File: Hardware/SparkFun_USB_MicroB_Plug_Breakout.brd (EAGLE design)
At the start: 22.9 x 14 mm, 3 parts

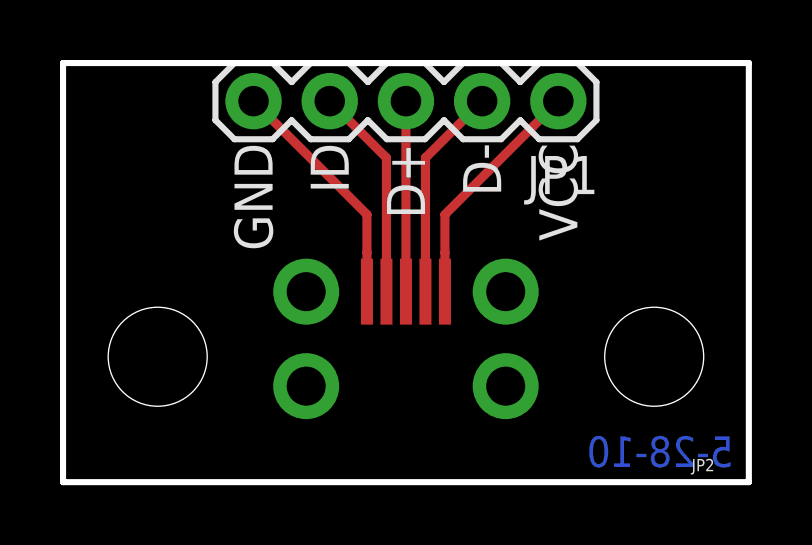
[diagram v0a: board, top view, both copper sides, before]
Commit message: Fixed USB Micro footprint.  Added OSHW SPK logo
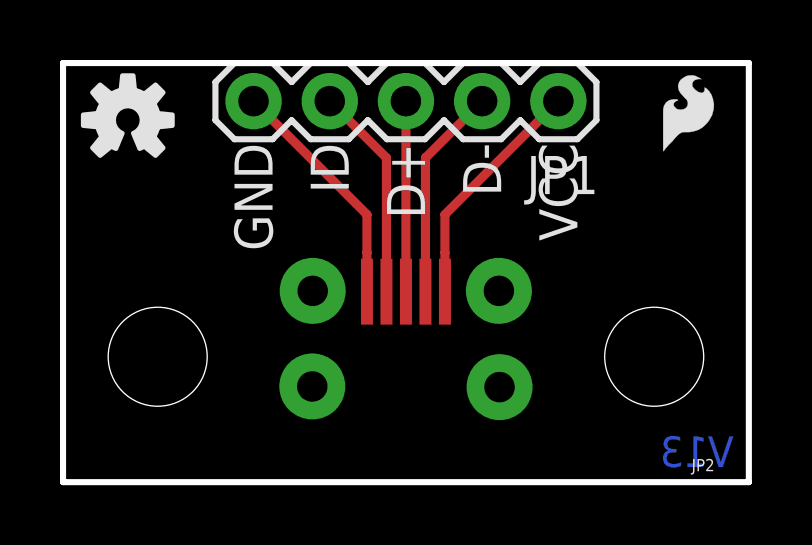
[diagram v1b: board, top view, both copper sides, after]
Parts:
- removed JP3: LOGO-SFESK, SparkFun:SFE-LOGO-FLAME
- added FRAME1: FRAME-LETTER, SparkFun-Aesthetics:CREATIVE_COMMONS
- added LOGO1: OSHW-LOGOS, SparkFun-Aesthetics:OSHW-LOGO-S
- added LOGO2: SFE_LOGO_FLAME.1_INCH, SparkFun-Aesthetics:SFE_LOGO_FLAME_.1
- JP2: value USB_MICROB_PLUG-SMT -> (none); device SparkFun:MICRO-B-SMT -> SparkFun-Connectors:MICRO-B-SMT
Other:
- board text added: "Breakout"
- board text added: "USB MicroB Plug"
- board text added: "V13"
- board text removed: "5-28-10"
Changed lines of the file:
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@@
 <?xml version="1.0" encoding="utf-8"?>
 <!DOCTYPE eagle SYSTEM "eagle.dtd">
-<eagle version="7.2.0">
+<eagle version="7.1.0">
 <drawing>
 <settings>
@@
 <layer number="54" name="bGND_GNDA" color="1" fill="9" visible="no" active="no"/>
 <layer number="56" name="wert" color="7" fill="1" visible="no" active="yes"/>
+<layer number="57" name="tCAD" color="7" fill="1" visible="no" active="no"/>
+<layer number="59" name="tCarbon" color="7" fill="1" visible="no" active="no"/>
+<layer number="60" name="bCarbon" color="7" fill="1" visible="no" active="no"/>
+<layer number="90" name="Modules" color="5" fill="1" visible="no" active="no"/>
 <layer number="91" name="Nets" color="2" fill="1" visible="no" active="no"/>
 <layer number="92" name="Busses" color="1" fill="1" visible="no" active="no"/>
@@
 <layer number="97" name="Info" color="7" fill="1" visible="no" active="no"/>
 <layer number="98" name="Guide" color="6" fill="1" visible="no" active="no"/>
+<layer number="99" name="SpiceOrder" color="7" fill="1" visible="no" active="no"/>
 <layer number="100" name="Muster" color="7" fill="1" visible="no" active="no"/>
 <layer number="101" name="Patch_Top" color="12" fill="4" visible="no" active="yes"/>
@@
 <layer number="106" name="bPlate" color="7" fill="1" visible="no" active="yes"/>
 <layer number="107" name="Crop" color="7" fill="1" visible="no" active="yes"/>
+<layer number="108" name="tplace-old" color="10" fill="1" visible="no" active="yes"/>
+<layer number="109" name="ref-old" color="11" fill="1" visible="no" active="yes"/>
+<layer number="110" name="fp0" color="7" fill="1" visible="no" active="yes"/>
+<layer number="111" name="LPC17xx" color="7" fill="1" visible="no" active="yes"/>
+<layer number="112" name="tSilk" color="7" fill="1" visible="no" active="yes"/>
+<layer number="113" name="IDFDebug" color="4" fill="1" visible="no" active="yes"/>
 <layer number="116" name="Patch_BOT" color="9" fill="4" visible="no" active="yes"/>
 <layer number="121" name="_tsilk" color="7" fill="1" visible="no" active="yes"/>
 <layer number="122" name="_bsilk" color="7" fill="1" visible="no" active="yes"/>
+<layer number="123" name="tTestmark" color="7" fill="1" visible="no" active="yes"/>
+<layer number="124" name="bTestmark" color="7" fill="1" visible="no" active="yes"/>
+<layer number="125" name="_tNames" color="7" fill="1" visible="no" active="yes"/>
+<layer number="126" name="_bNames" color="7" fill="1" visible="no" active="yes"/>
+<layer number="127" name="_tValues" color="7" fill="1" visible="no" active="yes"/>
+<layer number="128" name="_bValues" color="7" fill="1" visible="no" active="yes"/>
+<layer number="129" name="Mask" color="7" fill="1" visible="no" active="yes"/>
+<layer number="131" name="tAdjust" color="7" fill="1" visible="no" active="yes"/>
+<layer number="132" name="bAdjust" color="7" fill="1" visible="no" active="yes"/>
+<layer number="144" name="Drill_legend" color="7" fill="1" visible="no" active="yes"/>
+<layer number="150" name="Notes" color="7" fill="1" visible="no" active="yes"/>
 <layer number="151" name="HeatSink" color="7" fill="1" visible="no" active="yes"/>
+<layer number="152" name="_bDocu" color="7" fill="1" visible="no" active="yes"/>
+<layer number="153" name="FabDoc1" color="7" fill="1" visible="no" active="yes"/>
+<layer number="154" name="FabDoc2" color="7" fill="1" visible="no" active="yes"/>
+<layer number="155" name="FabDoc3" color="7" fill="1" visible="no" active="yes"/>
+<layer number="199" name="Contour" color="7" fill="1" visible="no" active="yes"/>
 <layer number="200" name="200bmp" color="1" fill="10" visible="no" active="yes"/>
 <layer number="201" name="201bmp" color="2" fill="10" visible="no" active="yes"/>
@@
 <layer number="207" name="207bmp" color="8" fill="10" visible="no" active="yes"/>
 <layer number="208" name="208bmp" color="9" fill="10" visible="no" active="yes"/>
+<layer number="209" name="209bmp" color="7" fill="1" visible="no" active="yes"/>
+<layer number="210" name="210bmp" color="7" fill="1" visible="no" active="yes"/>
+<layer number="211" name="211bmp" color="7" fill="1" visible="no" active="yes"/>
+<layer number="212" name="212bmp" color="7" fill="1" visible="no" active="yes"/>
+<layer number="213" name="213bmp" color="7" fill="1" visible="no" active="yes"/>
+<layer number="214" name="214bmp" color="7" fill="1" visible="no" active="yes"/>
+<layer number="215" name="215bmp" color="7" fill="1" visible="no" active="yes"/>
+<layer number="216" name="216bmp" color="7" fill="1" visible="no" active="yes"/>
+<layer number="217" name="217bmp" color="18" fill="1" visible="no" active="no"/>
+<layer number="218" name="218bmp" color="19" fill="1" visible="no" active="no"/>
+<layer number="219" name="219bmp" color="20" fill="1" visible="no" active="no"/>
+<layer number="220" name="220bmp" color="21" fill="1" visible="no" active="no"/>
+<layer number="221" name="221bmp" color="22" fill="1" visible="no" active="no"/>
+<layer number="222" name="222bmp" color="23" fill="1" visible="no" active="no"/>
+<layer number="223" name="223bmp" color="24" fill="1" visible="no" active="no"/>
+<layer number="224" name="224bmp" color="25" fill="1" visible="no" active="no"/>
+<layer number="225" name="225bmp" color="7" fill="1" visible="no" active="yes"/>
+<layer number="226" name="226bmp" color="7" fill="1" visible="no" active="yes"/>
+<layer number="227" name="227bmp" color="7" fill="1" visible="no" active="yes"/>
+<layer number="228" name="228bmp" color="7" fill="1" visible="no" active="yes"/>
+<layer number="229" name="229bmp" color="7" fill="1" visible="no" active="yes"/>
+<layer number="230" name="230bmp" color="7" fill="1" visible="no" active="yes"/>
+<layer number="231" name="231bmp" color="7" fill="1" visible="no" active="yes"/>
+<layer number="248" name="Housing" color="7" fill="1" visible="no" active="yes"/>
+<layer number="249" name="Edge" color="7" fill="1" visible="no" active="yes"/>
 <layer number="250" name="Descript" color="3" fill="1" visible="no" active="no"/>
 <layer number="251" name="SMDround" color="12" fill="11" visible="no" active="no"/>
 <layer number="254" name="cooling" color="7" fill="1" visible="no" active="yes"/>
+<layer number="255" name="routoute" color="7" fill="1" visible="no" active="yes"/>
 </layers>
 <board>
@@
 <text x="13.335" y="11.303" size="1.27" layer="21" font="vector" ratio="15" rot="R270">D-</text>
 <text x="15.875" y="11.303" size="1.27" layer="21" font="vector" ratio="15" rot="R270">VCC</text>
-<text x="22.352" y="0.508" size="1.016" layer="16" font="vector" ratio="15" rot="MR0">5-28-10</text>
+<text x="22.352" y="0.508" size="1.016" layer="16" font="vector" ratio="15" rot="MR0">V13</text>
 <text x="6.985" y="11.303" size="1.27" layer="22" font="vector" ratio="15" rot="MR270">GND</text>
 <text x="9.525" y="11.303" size="1.27" layer="22" font="vector" ratio="15" rot="MR270">ID</text>
@@
 <text x="14.605" y="11.303" size="1.27" layer="22" font="vector" ratio="15" rot="MR270">D-</text>
 <text x="17.145" y="11.303" size="1.27" layer="22" font="vector" ratio="15" rot="MR270">VCC</text>
+<text x="17.78" y="8.89" size="1.016" layer="22" font="vector" ratio="15" rot="MR0">USB MicroB Plug</text>
+<text x="14.732" y="7.747" size="1.016" layer="22" font="vector" ratio="15" rot="MR0">Breakout</text>
 </plain>
 <attributes>
@@
 <elements>
 <element name="JP1" library="SparkFun" package="1X05" value="" x="16.51" y="12.7" rot="R180"/>
-<element name="JP3" library="SparkFun" package="SFE-LOGO-FLAME" value="LOGO-SFESK" x="12.319" y="5.334" rot="MR0"/>
-<element name="JP2" library="SparkFun" package="MICRO-B-SMT" value="USB_MICROB_PLUG-SMT" x="11.43" y="6.35" rot="R180"/>
+<element name="JP2" library="SparkFun-Connectors" package="MICRO-B-SMT" value="" x="11.43" y="6.35" rot="R180"/>
+<element name="FRAME1" library="SparkFun-Aesthetics" package="CREATIVE_COMMONS" value="FRAME-LETTER" x="-15.36405625" y="-12.192"/>
+<element name="LOGO1" library="SparkFun-Aesthetics" package="OSHW-LOGO-S" value="OSHW-LOGOS" x="2.159" y="12.065"/>
+<element name="LOGO2" library="SparkFun-Aesthetics" package="SFE_LOGO_FLAME_.1" value="SFE_LOGO_FLAME.1_INCH" x="19.685" y="10.668"/>
 </elements>
 <signals>

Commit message: Added silk and prod attributes.
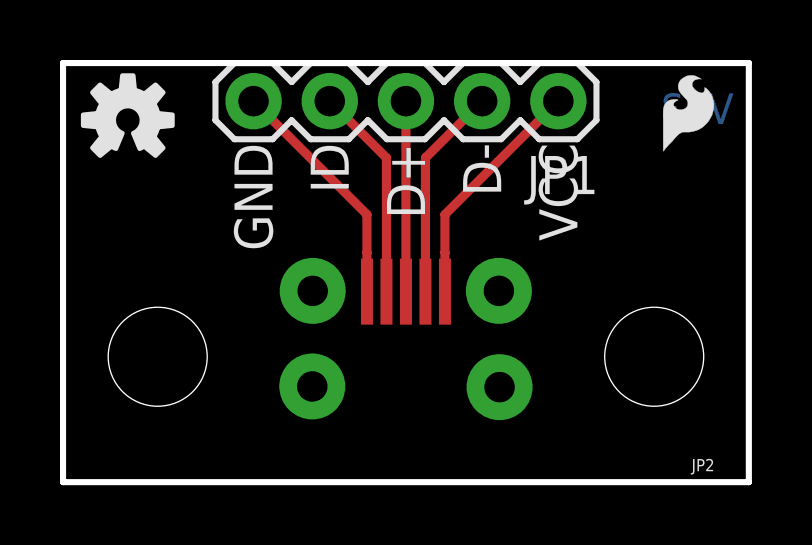
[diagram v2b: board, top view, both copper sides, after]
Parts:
- JP2: value (none) -> Micro B Plug
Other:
- board text added: "Jim Lindblom"
- board text added: "Revised by: Patrick Alberts"
- board text added: "USB MicroB Plug Breakout"
- board text removed: "Breakout"
- board text removed: "USB MicroB Plug"
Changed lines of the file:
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@@
 <layer number="23" name="tOrigins" color="15" fill="1" visible="yes" active="yes"/>
 <layer number="24" name="bOrigins" color="15" fill="1" visible="yes" active="yes"/>
-<layer number="25" name="tNames" color="7" fill="1" visible="no" active="yes"/>
+<layer number="25" name="tNames" color="7" fill="1" visible="yes" active="yes"/>
 <layer number="26" name="bNames" color="7" fill="1" visible="no" active="yes"/>
-<layer number="27" name="tValues" color="7" fill="1" visible="no" active="yes"/>
-<layer number="28" name="bValues" color="7" fill="1" visible="no" active="yes"/>
+<layer number="27" name="tValues" color="7" fill="1" visible="yes" active="yes"/>
+<layer number="28" name="bValues" color="7" fill="1" visible="yes" active="yes"/>
 <layer number="29" name="tStop" color="7" fill="3" visible="no" active="yes"/>
 <layer number="30" name="bStop" color="7" fill="6" visible="no" active="yes"/>
@@
 <text x="13.335" y="11.303" size="1.27" layer="21" font="vector" ratio="15" rot="R270">D-</text>
 <text x="15.875" y="11.303" size="1.27" layer="21" font="vector" ratio="15" rot="R270">VCC</text>
-<text x="22.352" y="0.508" size="1.016" layer="16" font="vector" ratio="15" rot="MR0">V13</text>
+<text x="22.352" y="11.938" size="1.016" layer="16" font="vector" ratio="15" rot="MR0">V13</text>
 <text x="6.985" y="11.303" size="1.27" layer="22" font="vector" ratio="15" rot="MR270">GND</text>
 <text x="9.525" y="11.303" size="1.27" layer="22" font="vector" ratio="15" rot="MR270">ID</text>
@@
 <text x="14.605" y="11.303" size="1.27" layer="22" font="vector" ratio="15" rot="MR270">D-</text>
 <text x="17.145" y="11.303" size="1.27" layer="22" font="vector" ratio="15" rot="MR270">VCC</text>
-<text x="17.78" y="8.89" size="1.016" layer="22" font="vector" ratio="15" rot="MR0">USB MicroB Plug</text>
-<text x="14.732" y="7.747" size="1.016" layer="22" font="vector" ratio="15" rot="MR0">Breakout</text>
+<text x="21.844" y="0.508" size="1.016" layer="22" font="vector" ratio="15" rot="MR0">USB MicroB Plug Breakout</text>
+<text x="-3.81" y="-15.24" size="1.778" layer="51" font="vector" ratio="10">Revised by: Patrick Alberts</text>
+<text x="14.732" y="-12.319" size="1.778" layer="51" font="vector" ratio="12">Jim Lindblom</text>
 </plain>
 <attributes>
@@
 <elements>
 <element name="JP1" library="SparkFun" package="1X05" value="" x="16.51" y="12.7" rot="R180"/>
-<element name="JP2" library="SparkFun-Connectors" package="MICRO-B-SMT" value="" x="11.43" y="6.35" rot="R180"/>
+<element name="JP2" library="SparkFun-Connectors" package="MICRO-B-SMT" value="Micro B Plug" x="11.43" y="6.35" rot="R180">
+<attribute name="PROD_ID" value="CONN-09900" x="11.43" y="6.35" size="1.778" layer="27" rot="R180" display="off"/>
+</element>
 <element name="FRAME1" library="SparkFun-Aesthetics" package="CREATIVE_COMMONS" value="FRAME-LETTER" x="-15.36405625" y="-12.192"/>
 <element name="LOGO1" library="SparkFun-Aesthetics" package="OSHW-LOGO-S" value="OSHW-LOGOS" x="2.159" y="12.065"/>

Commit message: Added Measures.
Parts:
- JP2: value Micro B Plug -> USB Micro B Plug
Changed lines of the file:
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@@
 <?xml version="1.0" encoding="utf-8"?>
 <!DOCTYPE eagle SYSTEM "eagle.dtd">
-<eagle version="7.1.0">
+<eagle version="6.4">
 <drawing>
 <settings>
@@
 <layer number="23" name="tOrigins" color="15" fill="1" visible="yes" active="yes"/>
 <layer number="24" name="bOrigins" color="15" fill="1" visible="yes" active="yes"/>
-<layer number="25" name="tNames" color="7" fill="1" visible="yes" active="yes"/>
+<layer number="25" name="tNames" color="7" fill="1" visible="no" active="yes"/>
 <layer number="26" name="bNames" color="7" fill="1" visible="no" active="yes"/>
-<layer number="27" name="tValues" color="7" fill="1" visible="yes" active="yes"/>
-<layer number="28" name="bValues" color="7" fill="1" visible="yes" active="yes"/>
+<layer number="27" name="tValues" color="7" fill="1" visible="no" active="yes"/>
+<layer number="28" name="bValues" color="7" fill="1" visible="no" active="yes"/>
 <layer number="29" name="tStop" color="7" fill="3" visible="no" active="yes"/>
 <layer number="30" name="bStop" color="7" fill="6" visible="no" active="yes"/>
@@
 <layer number="45" name="Holes" color="7" fill="1" visible="yes" active="yes"/>
 <layer number="46" name="Milling" color="3" fill="1" visible="no" active="yes"/>
-<layer number="47" name="Measures" color="7" fill="1" visible="no" active="yes"/>
+<layer number="47" name="Measures" color="7" fill="1" visible="yes" active="yes"/>
 <layer number="48" name="Document" color="7" fill="1" visible="no" active="yes"/>
 <layer number="49" name="Reference" color="7" fill="1" visible="no" active="yes"/>
@@
 <text x="-3.81" y="-15.24" size="1.778" layer="51" font="vector" ratio="10">Revised by: Patrick Alberts</text>
 <text x="14.732" y="-12.319" size="1.778" layer="51" font="vector" ratio="12">Jim Lindblom</text>
+<dimension x1="-3.81" y1="0" x2="-3.81" y2="13.97" x3="-5.08" y3="6.985" textsize="1.778" textratio="15" layer="47" unit="inch" visible="yes"/>
+<dimension x1="0" y1="17.78" x2="22.86" y2="17.78" x3="11.43" y3="16.51" textsize="1.778" textratio="15" layer="47" unit="inch" visible="yes"/>
 </plain>
 <attributes>
@@
 <pass name="Default">
 <param name="RoutingGrid" value="50mil"/>
-<param name="AutoGrid" value="1"/>
-<param name="Efforts" value="0"/>
-<param name="TopRouterVariant" value="1"/>
 <param name="tpViaShape" value="round"/>
 <param name="PrefDir.1" value="|"/>
@@
 <elements>
 <element name="JP1" library="SparkFun" package="1X05" value="" x="16.51" y="12.7" rot="R180"/>
-<element name="JP2" library="SparkFun-Connectors" package="MICRO-B-SMT" value="Micro B Plug" x="11.43" y="6.35" rot="R180">
+<element name="JP2" library="SparkFun-Connectors" package="MICRO-B-SMT" value="USB Micro B Plug" x="11.43" y="6.35" rot="R180">
 <attribute name="PROD_ID" value="CONN-09900" x="11.43" y="6.35" size="1.778" layer="27" rot="R180" display="off"/>
 </element>
